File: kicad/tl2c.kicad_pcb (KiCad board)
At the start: 4 copper layers, 119.4 x 127 mm, 86 parts, among them IC101 ATTINY20-X, P101 12VDC, P102 I2C Master, P103 Spare, P104 ISP Header, P105 LED_DRIVER, P106 240VAC, P107 LED_DRIVER, P108 LED_OUT, P301 PIR13, Q301 IRLML2502, Q302 IRLML2502, Q303 IRLML2502, Q401 IRLML2502, Q402 IRLML2502, Q403 IRLML2502, SW101 TL3315NF160Q, U201 LF120ABDT-TR, U202 TPS70933

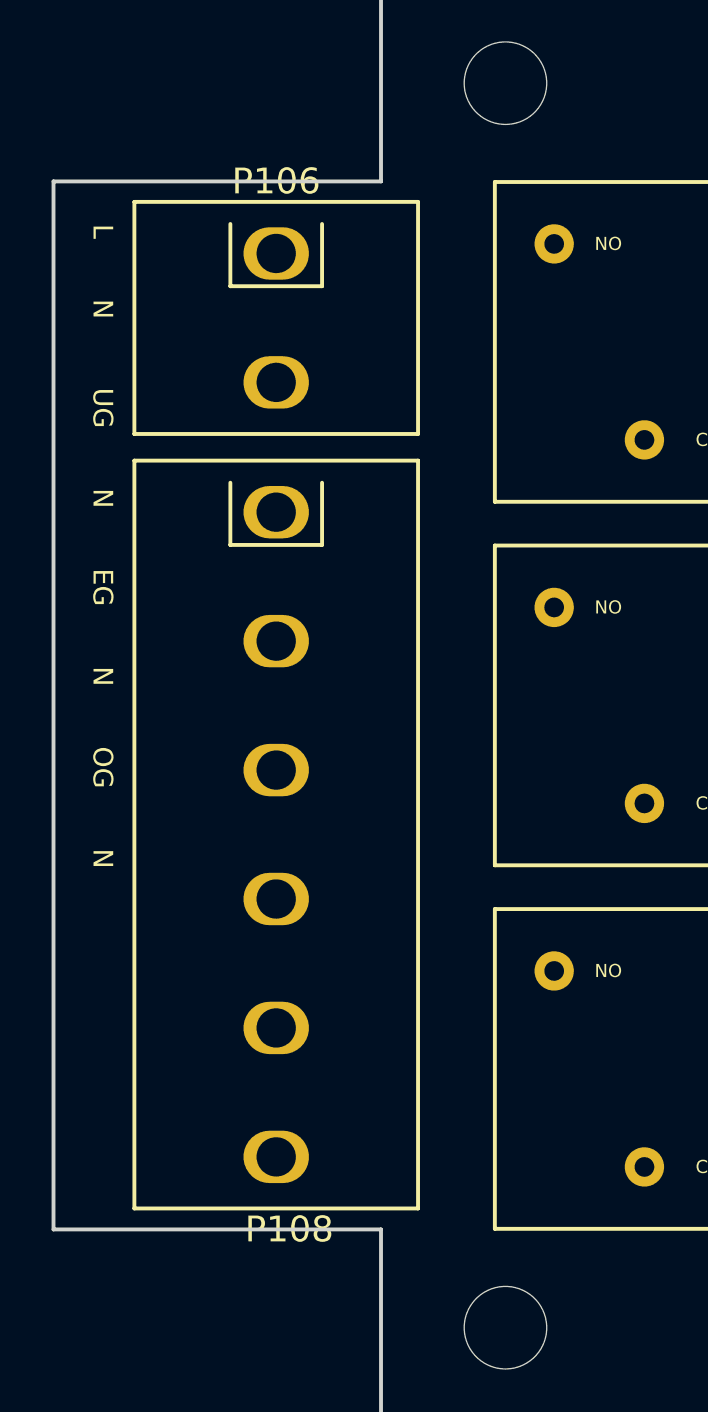
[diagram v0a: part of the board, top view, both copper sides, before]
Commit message: More rework on the board for the correct terminal blocks and case
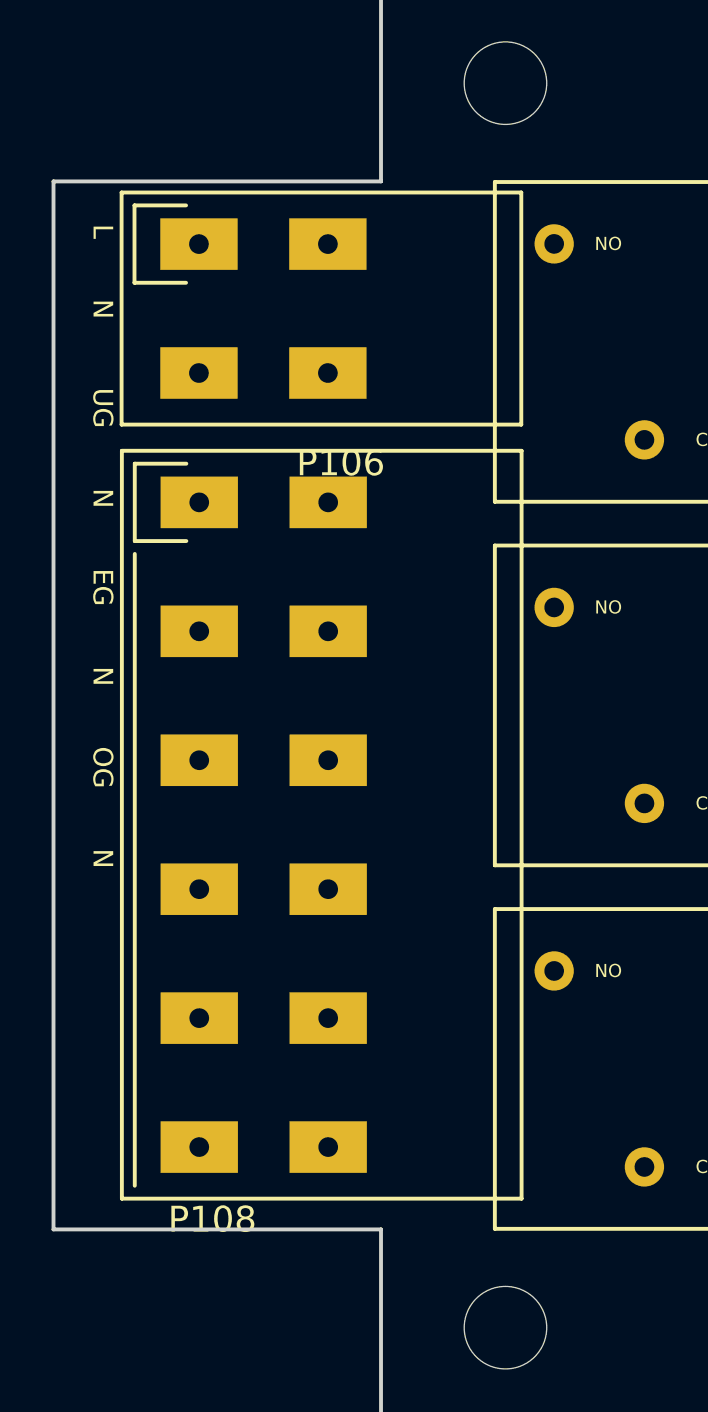
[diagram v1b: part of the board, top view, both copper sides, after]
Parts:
- moved P106 3.02 mm to (53.9, 41.8)
- moved P108 3.01 mm to (53.9, 51.8)
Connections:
- SW101 pad 2: (no net) -> Net-(SW101-Pad2)
- SW101 pad 4: (no net) -> Net-(SW101-Pad4)
- U202 pad 4: (no net) -> Net-(U202-Pad4)
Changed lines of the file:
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@@
 (kicad_pcb (version 4) (host pcbnew 4.0.2-4+6225~38~ubuntu14.04.1-stable)
   (general
-    (links 145)
-    (no_connects 41)
-    (area 34.319287 10.866 177.773001 170.915001)
+    (links 153)
+    (no_connects 49)
+    (area 48.184999 30.404999 167.715001 157.555001)
     (thickness 1.6)
     (drawings 58)
@@
     (zones 0)
     (modules 86)
-    (nets 50)
+    (nets 53)
   )
   (page A4)
@@
     (pad_to_mask_clearance 0.2)
     (aux_axis_origin 0 0)
-    (visible_elements FFFEEFFF)
+    (visible_elements FFFEFFFF)
     (pcbplotparams
       (layerselection 0x010fc_80000007)
@@
   (net 48 "Net-(D201-Pad2)")
   (net 49 "Net-(D202-Pad2)")
+  (net 50 "Net-(SW101-Pad2)")
+  (net 51 "Net-(SW101-Pad4)")
+  (net 52 "Net-(U202-Pad4)")
   (net_class Default "This is the default net class."
     (clearance 0.1524)
@@
     (add_net "Net-(Q403-Pad3)")
     (add_net "Net-(R202-Pad1)")
+    (add_net "Net-(SW101-Pad2)")
+    (add_net "Net-(SW101-Pad4)")
+    (add_net "Net-(U202-Pad4)")
   )
   (module Measurement_Points:Measurement_Point_Round-SMD-Pad_Small (layer F.Cu)
@@
     (pad 1 smd rect (at -3.2 -1.9 270) (size 1.6 1) (layers F.Cu F.Paste F.Mask)
       (net 11 /Reset))
-    (pad 2 smd rect (at 3.2 -1.9 270) (size 1.6 1) (layers F.Cu F.Paste F.Mask))
+    (pad 2 smd rect (at 3.2 -1.9 270) (size 1.6 1) (layers F.Cu F.Paste F.Mask)
+      (net 50 "Net-(SW101-Pad2)"))
     (pad 3 smd rect (at -3.2 1.9 270) (size 1.6 1) (layers F.Cu F.Paste F.Mask)
       (net 1 GND))
-    (pad 4 smd rect (at 3.2 1.9 270) (size 1.6 1) (layers F.Cu F.Paste F.Mask))
+    (pad 4 smd rect (at 3.2 1.9 270) (size 1.6 1) (layers F.Cu F.Paste F.Mask)
+      (net 51 "Net-(SW101-Pad4)"))
   )
   (module Measurement_Points:Measurement_Point_Round-SMD-Pad_Small (layer F.Cu)
@@
     (pad 5 smd rect (at -0.95 -1.35) (size 0.74 1.19) (layers F.Cu F.Paste F.Mask)
       (net 36 /PIR13/Ub+))
-    (pad 4 smd rect (at 0.95 -1.35) (size 0.74 1.19) (layers F.Cu F.Paste F.Mask))
+    (pad 4 smd rect (at 0.95 -1.35) (size 0.74 1.19) (layers F.Cu F.Paste F.Mask)
+      (net 52 "Net-(U202-Pad4)"))
     (pad 2 smd rect (at 0 1.35) (size 0.74 1.19) (layers F.Cu F.Paste F.Mask)
       (net 1 GND))
@@
     (pad 1 np_thru_hole circle (at 0 0) (size 3.2 3.2) (drill 3.2) (layers *.Cu *.Mask))
   )
-  (module tl2c-footprint:Spring_Terminal_Block_1_x_2_5mm (layer F.Cu)
-    (at 56.896 42.164)
-    (fp_text reference P106 (at 0 -2.794) (layer F.SilkS)
-      (effects (font (size 1 1) (thickness 0.15)))
-    )
-    (fp_text value 240VAC (at 0 -5) (layer F.Fab)
-      (effects (font (size 1 1) (thickness 0.15)))
-    )
-    (fp_line (start -1.778 -1.143) (end -1.778 1.27) (layer F.SilkS) (width 0.15))
-    (fp_line (start -1.778 1.27) (end 1.778 1.27) (layer F.SilkS) (width 0.15))
-    (fp_line (start 1.778 1.27) (end 1.778 -1.143) (layer F.SilkS) (width 0.15))
-    (fp_line (start -5.5 -2) (end 5.5 -2) (layer F.SilkS) (width 0.15))
-    (fp_line (start 5.5 -2) (end 5.5 7) (layer F.SilkS) (width 0.15))
-    (fp_line (start 5.5 7) (end -5.5 7) (layer F.SilkS) (width 0.15))
-    (fp_line (start -5.5 7) (end -5.5 -2) (layer F.SilkS) (width 0.15))
-    (pad 1 thru_hole oval (at 0 0) (size 2.54 2.032) (drill 1.524) (layers *.Cu *.Mask)
-      (net 20 /Lin))
-    (pad 2 thru_hole oval (at 0 5) (size 2.54 2.032) (drill 1.524) (layers *.Cu *.Mask)
-      (net 21 /Neutral))
-  )
-  (module tl2c-footprint:Spring_Terminal_Block_1_x_6_5mm (layer F.Cu)
-    (at 56.896 52.197)
-    (fp_text reference P108 (at 0.508 27.813) (layer F.SilkS)
-      (effects (font (size 1 1) (thickness 0.15)))
-    )
-    (fp_text value LED_OUT (at 0 -3.5) (layer F.Fab)
-      (effects (font (size 1 1) (thickness 0.15)))
-    )
-    (fp_line (start -1.778 -1.143) (end -1.778 1.27) (layer F.SilkS) (width 0.15))
-    (fp_line (start -1.778 1.27) (end 1.778 1.27) (layer F.SilkS) (width 0.15))
-    (fp_line (start 1.778 1.27) (end 1.778 -1.143) (layer F.SilkS) (width 0.15))
-    (fp_line (start -5.5 -2) (end 5.5 -2) (layer F.SilkS) (width 0.15))
-    (fp_line (start 5.5 -2) (end 5.5 27) (layer F.SilkS) (width 0.15))
-    (fp_line (start 5.5 27) (end -5.5 27) (layer F.SilkS) (width 0.15))
-    (fp_line (start -5.5 27) (end -5.5 -2) (layer F.SilkS) (width 0.15))
-    (pad 1 thru_hole oval (at 0 0) (size 2.54 2.032) (drill 1.524) (layers *.Cu *.Mask)
-      (net 22 /LineUG))
-    (pad 2 thru_hole oval (at 0 5) (size 2.54 2.032) (drill 1.524) (layers *.Cu *.Mask)
-      (net 21 /Neutral))
-    (pad 3 thru_hole oval (at 0 10) (size 2.54 2.032) (drill 1.524) (layers *.Cu *.Mask)
-      (net 23 /LineEG))
-    (pad 4 thru_hole oval (at 0 15) (size 2.54 2.032) (drill 1.524) (layers *.Cu *.Mask F.SilkS)
-      (net 21 /Neutral))
-    (pad 5 thru_hole oval (at 0 20) (size 2.54 2.032) (drill 1.524) (layers *.Cu *.Mask F.SilkS)
-      (net 24 /LineOG))
-    (pad 6 thru_hole oval (at 0 25) (size 2.54 2.032) (drill 1.524) (layers *.Cu *.Mask F.SilkS)
-      (net 21 /Neutral))
-  )
   (module Symbols:KiCad-Logo2_6mm_SilkScreen (layer F.Cu)
     (at 113.03 161.29)
@@
       (xy -2.537313 -2.939947) (xy -2.454562 -2.96715) (xy -2.376928 -2.977424) (xy -2.273043 -2.973429)) (layer F.SilkS) (width 0.01))
   )
+  (module tl2c-footprint:Spring_Terminal_Block_1_x_6_5mm (layer F.Cu)
+    (at 53.9115 51.816)
+    (fp_text reference P108 (at 0.508 27.813) (layer F.SilkS)
+      (effects (font (size 1 1) (thickness 0.15)))
+    )
+    (fp_text value LED_OUT (at 0 -3.5) (layer F.Fab)
+      (effects (font (size 1 1) (thickness 0.15)))
+    )
+    (fp_line (start -2.5 2) (end -2.5 26.5) (layer F.SilkS) (width 0.15))
+    (fp_line (start -0.5 -1.5) (end -2.5 -1.5) (layer F.SilkS) (width 0.15))
+    (fp_line (start -2.5 -1.5) (end -2.5 1.5) (layer F.SilkS) (width 0.15))
+    (fp_line (start -2.5 1.5) (end -0.5 1.5) (layer F.SilkS) (width 0.15))
+    (fp_line (start -3 -2) (end 12.5 -2) (layer F.SilkS) (width 0.15))
+    (fp_line (start 12.5 -2) (end 12.5 27) (layer F.SilkS) (width 0.15))
+    (fp_line (start 12.5 27) (end -3 27) (layer F.SilkS) (width 0.15))
+    (fp_line (start -3 27) (end -3 -2) (layer F.SilkS) (width 0.15))
+    (pad 1 thru_hole rect (at 0 0) (size 3 2) (drill 0.762) (layers *.Cu *.Mask F.SilkS)
+      (net 22 /LineUG))
+    (pad 2 thru_hole rect (at 0 5) (size 3 2) (drill 0.762) (layers *.Cu *.Mask F.SilkS)
+      (net 21 /Neutral))
+    (pad 3 thru_hole rect (at 0 10) (size 3 2) (drill 0.762) (layers *.Cu *.Mask F.SilkS)
+      (net 23 /LineEG))
+    (pad 4 thru_hole rect (at 0 15) (size 3 2) (drill 0.762) (layers *.Cu *.Mask F.SilkS)
+      (net 21 /Neutral))
+    (pad 5 thru_hole rect (at 0 20) (size 3 2) (drill 0.762) (layers *.Cu *.Mask F.SilkS)
+      (net 24 /LineOG))
+    (pad 6 thru_hole rect (at 0 25) (size 3 2) (drill 0.762) (layers *.Cu *.Mask F.SilkS)
+      (net 21 /Neutral))
+    (pad 7 thru_hole rect (at 5 25) (size 3 2) (drill 0.762) (layers *.Cu *.Mask F.SilkS)
+      (net 21 /Neutral))
+    (pad 8 thru_hole rect (at 5 20) (size 3 2) (drill 0.762) (layers *.Cu *.Mask F.SilkS)
+      (net 24 /LineOG))
+    (pad 9 thru_hole rect (at 5 15) (size 3 2) (drill 0.762) (layers *.Cu *.Mask F.SilkS)
+      (net 21 /Neutral))
+    (pad 10 thru_hole rect (at 5 10) (size 3 2) (drill 0.762) (layers *.Cu *.Mask F.SilkS)
+      (net 23 /LineEG))
+    (pad 11 thru_hole rect (at 5 5) (size 3 2) (drill 0.762) (layers *.Cu *.Mask F.SilkS)
+      (net 21 /Neutral))
+    (pad 12 thru_hole rect (at 5 0) (size 3 2) (drill 0.762) (layers *.Cu *.Mask F.SilkS)
+      (net 22 /LineUG))
+  )
+  (module tl2c-footprint:Spring_Terminal_Block_1_x_2_5mm (layer F.Cu)
+    (at 53.9 41.8)
+    (fp_text reference P106 (at 5.5 8.5) (layer F.SilkS)
+      (effects (font (size 1 1) (thickness 0.15)))
+    )
+    (fp_text value 240VAC (at 6 -3.5) (layer F.Fab)
+      (effects (font (size 1 1) (thickness 0.15)))
+    )
+    (fp_line (start 12.5 -2) (end 12.5 7) (layer F.SilkS) (width 0.15))
+    (fp_line (start -3 -2) (end -3 7) (layer F.SilkS) (width 0.15))
+    (fp_line (start -0.5 -1.5) (end -2.5 -1.5) (layer F.SilkS) (width 0.15))
+    (fp_line (start -2.5 -1.5) (end -2.5 1.5) (layer F.SilkS) (width 0.15))
+    (fp_line (start -2.5 1.5) (end -0.5 1.5) (layer F.SilkS) (width 0.15))
+    (fp_line (start -3 -2) (end 12.5 -2) (layer F.SilkS) (width 0.15))
+    (fp_line (start 12.5 7) (end -3 7) (layer F.SilkS) (width 0.15))
+    (pad 1 thru_hole rect (at 0 0) (size 3 2) (drill 0.762) (layers *.Cu *.Mask F.SilkS)
+      (net 20 /Lin))
+    (pad 2 thru_hole rect (at 0 5) (size 3 2) (drill 0.762) (layers *.Cu *.Mask F.SilkS)
+      (net 21 /Neutral))
+    (pad 3 thru_hole rect (at 5 5) (size 3 2) (drill 0.762) (layers *.Cu *.Mask F.SilkS)
+      (net 21 /Neutral))
+    (pad 4 thru_hole rect (at 5 0) (size 3 2) (drill 0.762) (layers *.Cu *.Mask F.SilkS)
+      (net 20 /Lin))
+  )
   (dimension 58.42 (width 0.3) (layer Eco1.User)

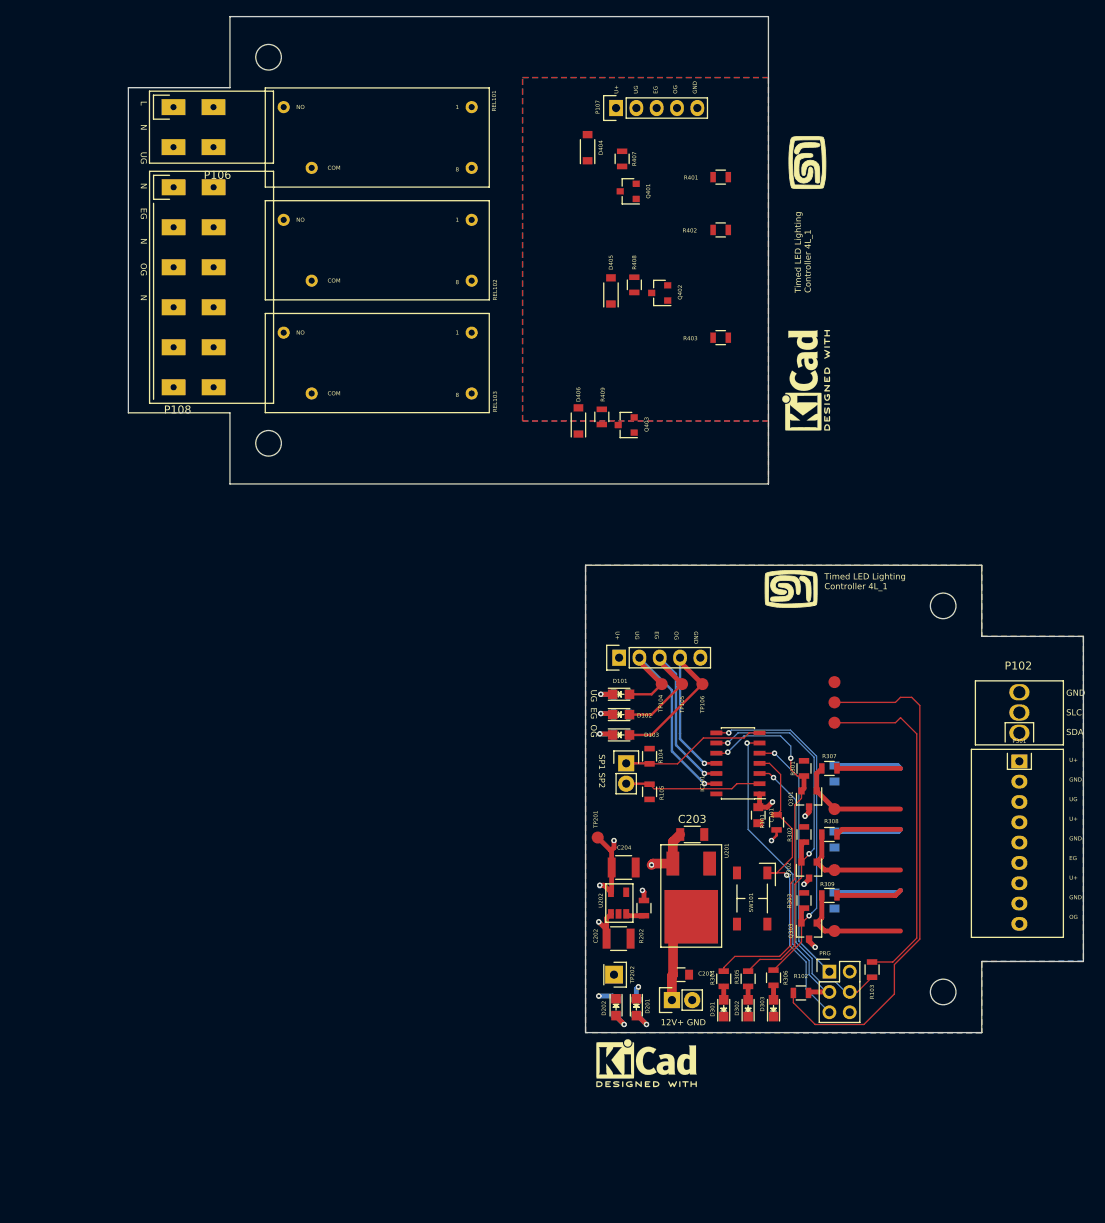
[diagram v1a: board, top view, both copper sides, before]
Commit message: More layout re-work and footprint changes
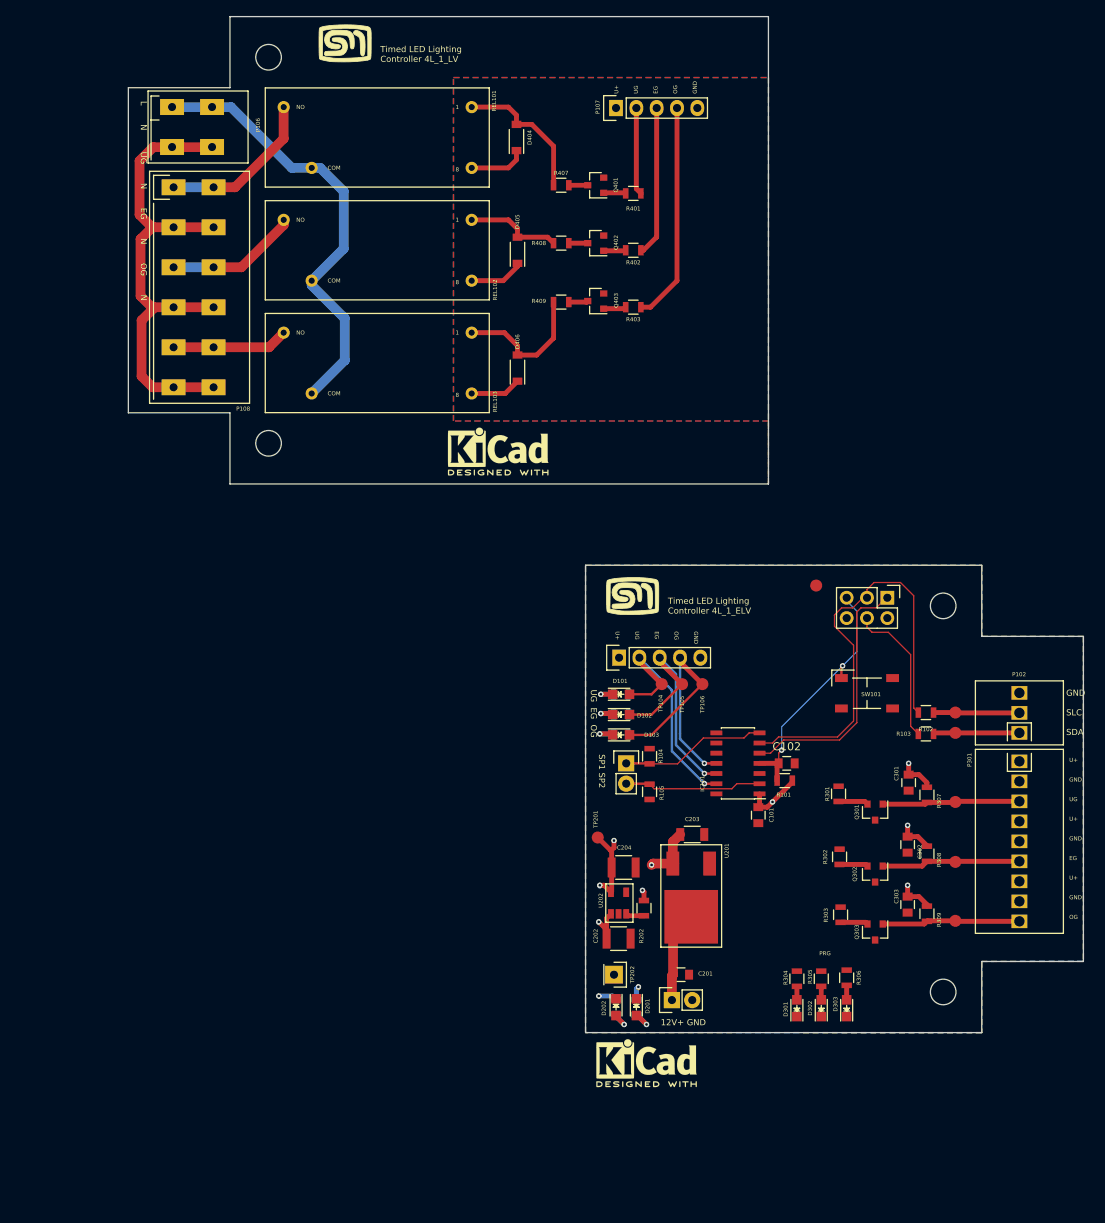
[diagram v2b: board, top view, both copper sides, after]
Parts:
- added C102: 100n 50V, Capacitors_SMD:C_0805, F.Cu at (130.6, 123.8)
- C101: value 100n 10V -> 100n 50V
- C301, C302, C303: moved to F.Cu
- P106: footprint tl2c-footprint:Spring_Terminal_Block_1_x_2_5mm -> tl2c-footprint:TERMINAL_BLOCK_2_5MM_5MM
- P108: footprint tl2c-footprint:Spring_Terminal_Block_1_x_6_5mm -> tl2c-footprint:TERMINAL_BLOCK_6_5MM_5MM
- moved G*** 59.7 mm to (75.3, 33.8), turned to 0 degrees
- moved P104 47.3 mm to (143.1, 103.1), turned to 270 degrees
- moved REF*** 39.5 mm to (94.5, 84.8), turned to 0 degrees
- moved R102 38.4 mm to (148.0, 117.5), turned to 180 degrees
- moved R103 30.2 mm to (148.0, 120.1), turned to 180 degrees
- moved SW101 29.4 mm to (140.6, 115.1), turned to 0 degrees
- moved G*** 19.8 mm to (111.3, 102.9)
- moved Q403 16.0 mm to (106.7, 66.0)
- moved R409 15.2 mm to (102.4, 66.2), turned to 0 degrees
- moved TP102 15.2 mm to (151.6, 117.5)
- moved TP103 15.2 mm to (151.6, 120.0)
- moved TP303 15.2 mm to (151.6, 143.5)
- moved TP302 15.1 mm to (151.6, 136.1)
- moved TP301 15.1 mm to (151.6, 128.7)
- moved D405 12.7 mm to (96.9, 59.7)
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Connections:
- net /Reset renamed /~Reset
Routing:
- net /Neutral: track 0.00 -> 64.5 mm, vias 0 -> 1
- net /Lin: track 0.00 -> 56.0 mm
- net /SCL: track 66.0 -> 10.8 mm
- net /PIR13/SIG_EG: track 48.3 -> 3.58 mm, vias 2 -> 0
- net /PIR13/SIG_UG: track 48.1 -> 4.43 mm, vias 2 -> 0
- net /PIR13/SIG_OG: track 45.0 -> 3.45 mm, vias 2 -> 0
- net /PIR13/U+: track 65.7 -> 29.7 mm, vias 4 -> 7
- net /SDA: track 43.7 -> 10.8 mm
- net /LED Driver/Relay_OG: track 0.00 -> 27.5 mm
- net /LED Driver/LED_DRIVER_U+: track 0.00 -> 20.4 mm
- net /LineUG: track 0.00 -> 20.2 mm
- net /MOSI: track 37.7 -> 18.3 mm, vias 1 -> 0
- net /LED Driver/Relay_EG: track 0.00 -> 18.8 mm
- net Net-(D404-Pad2): track 0.00 -> 17.8 mm
- net Net-(D406-Pad2): track 0.00 -> 17.5 mm
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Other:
- board text added: "Timed LED Lighting Controller 4L_1_ELV"
- board text added: "Timed LED Lighting Controller 4L_1_LV"
- board text removed: "Timed LED Lighting Controller 4L_1"
